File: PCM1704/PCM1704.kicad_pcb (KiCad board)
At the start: 4 copper layers, 90 x 90 mm, 126 parts, among them IC1 LT3042, IC2 LT3042, J1 AUDIO OUT, J2 POWER, J3 PROG, J5 I2S IN, U1 PCM1704, U10 LM337, U12 LM317, U2 PCM1704, U3 DF1704, U4 OPA1611, U5 OPA1611, U6 LT3094, U7 ATtiny1614, U8 OPA1612, U9 OPA1612

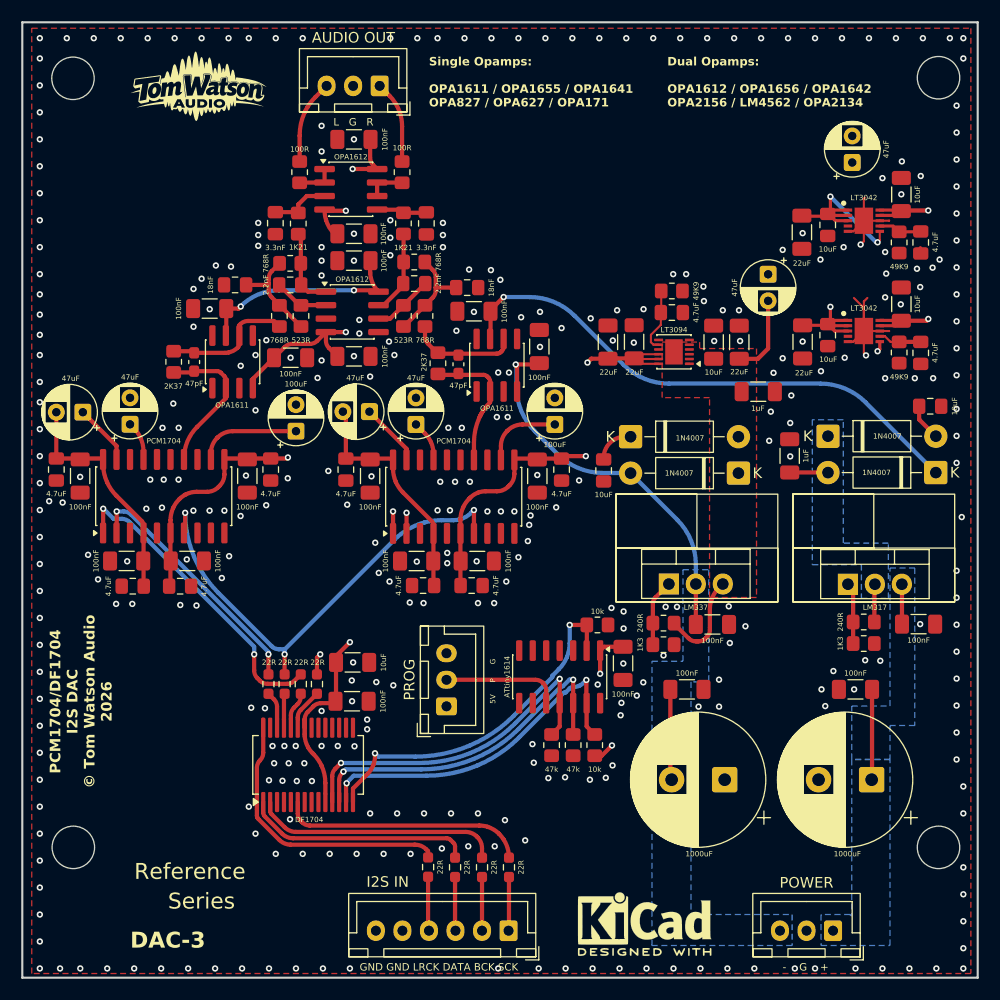
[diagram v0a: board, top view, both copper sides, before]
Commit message: PCM1704: snapshot before XMOS receive-buffer schematic changes
Adds DESIGN_REVIEW.md (performance review) and a manual zip backup.

Co-Authored-By: Claude Opus 5.5 <noreply@anthropic.com>
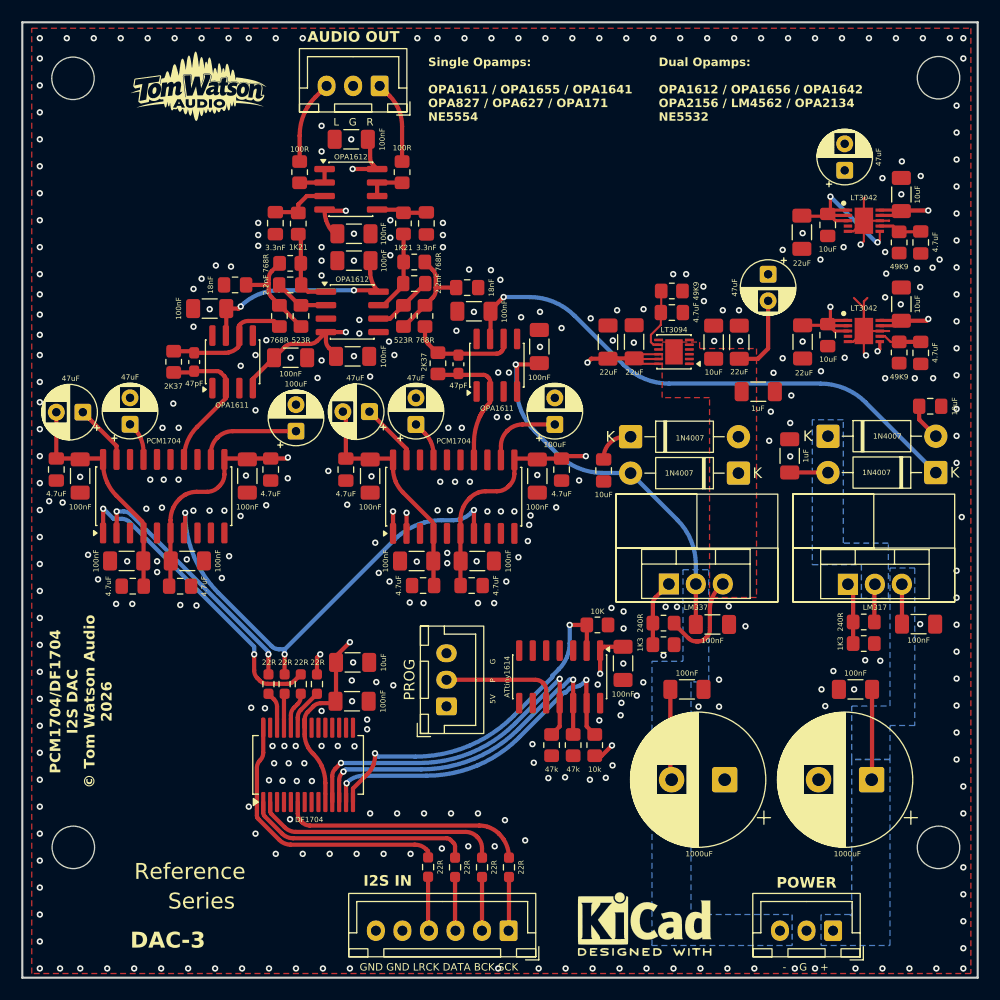
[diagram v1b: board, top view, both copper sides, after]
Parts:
- R75: value 10k -> 10K
- moved C22 1.02 mm to (188.2, 67.7)
- moved C86 0.25 mm to (141.7, 64.8)
- moved C85 0.13 mm to (141.9, 85.2)
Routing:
- net /+5VDF: track 165.0 -> 143.5 mm
- net /+8V: track 65.7 -> 64.2 mm
- net GND: track 22.4 -> 22.3 mm, vias 357 -> 358
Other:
- board text added: "Dual Opamps: OPA1612 / OPA1656 / OPA1642 OPA2156 / LM4562 / OPA2134 NE5532"
- board text added: "Single Opamps: OPA1611 / OPA1655 / OPA1641 OPA827 / OPA627 / OPA171 NE5554"
- board text removed: "Dual Opamps: OPA1612 / OPA1656 / OPA1642 OPA2156 / LM4562 / OPA2134"
- board text removed: "Single Opamps: OPA1611 / OPA1655 / OPA1641 OPA827 / OPA627 / OPA171"

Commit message: PCM1704: XMOS receive buffer, GND vias, WCLK re-route, 68R DF1704 series resistors
- Add U11 (74LVC1G17) MCLK Schmitt buffer, U13 (74LVC125APW) for BCK/DATA/LRCK,
  U14 (TPS7A2033) 3V3 rail; DF1704 inputs renamed DF_*
- GND vias at new ICs and decoupling caps; fix U13 pad 10 clearance
- Re-route WCLK on B.Cu so it no longer runs under BCLK on In2
- R79-R82 22R -> 68R (DF1704 SBAS099A 50-100R guidance), note updated
- DESIGN_REVIEW.md: H3 decision, LT3094 verification, change log

Co-Authored-By: Claude Opus 5.5 <noreply@anthropic.com>
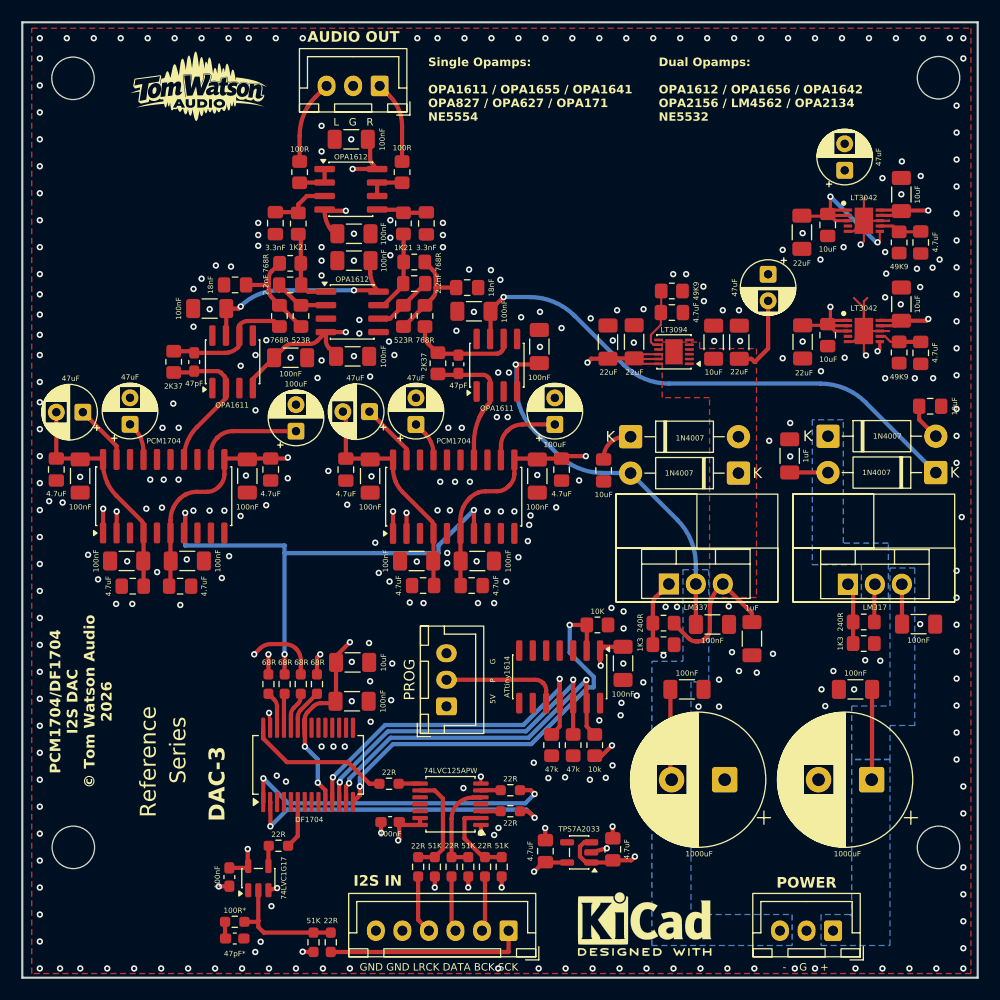
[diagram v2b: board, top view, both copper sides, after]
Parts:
- added C108: 100nF, Capacitor_SMD:C_0603_1608Metric_Pad1.08x0.95mm_HandSolder, F.Cu at (130.3, 134.3)
- added C109: 100nF, Capacitor_SMD:C_0603_1608Metric_Pad1.08x0.95mm_HandSolder, F.Cu at (145.4, 129.1)
- added C110: 4.7uF, Capacitor_SMD:C_0805_2012Metric_Pad1.18x1.45mm_HandSolder, F.Cu at (166.4, 131.7)
- added C111: 4.7uF, Capacitor_SMD:C_0805_2012Metric_Pad1.18x1.45mm_HandSolder, F.Cu at (160.0, 131.8)
- added C112: 47pF*, Capacitor_SMD:C_0603_1608Metric_Pad1.08x0.95mm_HandSolder, F.Cu at (130.8, 140.1)
- added R83: 51K, Resistor_SMD:R_0603_1608Metric_Pad0.98x0.95mm_HandSolder, F.Cu at (138.2, 140.4)
- added R84: 51K, Resistor_SMD:R_0603_1608Metric_Pad0.98x0.95mm_HandSolder, F.Cu at (155.9, 133.3)
- added R85: 51K, Resistor_SMD:R_0603_1608Metric_Pad0.98x0.95mm_HandSolder, F.Cu at (152.8, 133.3)
- added R86: 51K, Resistor_SMD:R_0603_1608Metric_Pad0.98x0.95mm_HandSolder, F.Cu at (149.6, 133.3)
- added R87: 22R, Resistor_SMD:R_0603_1608Metric_Pad0.98x0.95mm_HandSolder, F.Cu at (134.9, 131.3)
- added R88: 22R, Resistor_SMD:R_0603_1608Metric_Pad0.98x0.95mm_HandSolder, F.Cu at (156.7, 128.1)
- added R89: 22R, Resistor_SMD:R_0603_1608Metric_Pad0.98x0.95mm_HandSolder, F.Cu at (156.7, 126.1)
- added R90: 22R, Resistor_SMD:R_0603_1608Metric_Pad0.98x0.95mm_HandSolder, F.Cu at (145.3, 125.5)
- added R91: 100R*, Resistor_SMD:R_0603_1608Metric_Pad0.98x0.95mm_HandSolder, F.Cu at (130.8, 138.5)
- added U11: 74LVC1G17, Package_TO_SOT_SMD:SOT-23-5, F.Cu at (133.0, 134.4)
- added U13: 74LVC125APW, Package_SO:TSSOP-14_4.4x5mm_P0.65mm, F.Cu at (151.1, 127.4)
- added U14: TPS7A2033, Package_TO_SOT_SMD:SOT-23-5, F.Cu at (163.2, 131.9)
- R79, R80, R81, R82: value 22R -> 68R
- moved C90 23.3 mm to (179.5, 111.8), turned to -90 degrees
- moved R31 18.2 mm to (139.8, 140.4)
- moved R28 0.94 mm to (148.0, 133.3)
- moved R29 0.33 mm to (151.2, 133.3)
- moved R30 0.28 mm to (154.3, 133.3)
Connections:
- U3 pad 1: /DATAIN -> /DF_DIN
- U3 pad 2: /BCKIN -> /DF_BCK
- U3 pad 28: /LRCKIN -> /DF_LRCK
- U3 pad 6: /SCKIN -> /DF_SCK
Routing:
- net /+3V3: track 0.00 -> 42.0 mm, vias 0 -> 3
- net /DF_DIN: track 0.00 -> 30.6 mm, vias 0 -> 2
- net /DF_BCK: track 0.00 -> 29.8 mm, vias 0 -> 2
- net /+5VDF: track 143.5 -> 162.6 mm, vias 4 -> 7
- net /LRCKIN: track 27.2 -> 9.88 mm
- net /BCKIN: track 23.4 -> 7.69 mm
- net /DF_LRCK: track 0.00 -> 13.7 mm
- net Net-(J5-Pin_1): track 5.07 -> 18.8 mm
- net GND: track 22.3 -> 35.9 mm, vias 358 -> 343
- net /DATAIN: track 21.5 -> 9.02 mm
- net /SCKIN: track 23.4 -> 11.9 mm
- net /-8V: track 18.3 -> 23.3 mm
- net /DF_RST: track 34.2 -> 39.0 mm
- net /DF_SCK: track 0.00 -> 4.50 mm
- net Net-(U1-WCLK): track 46.1 -> 48.7 mm
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
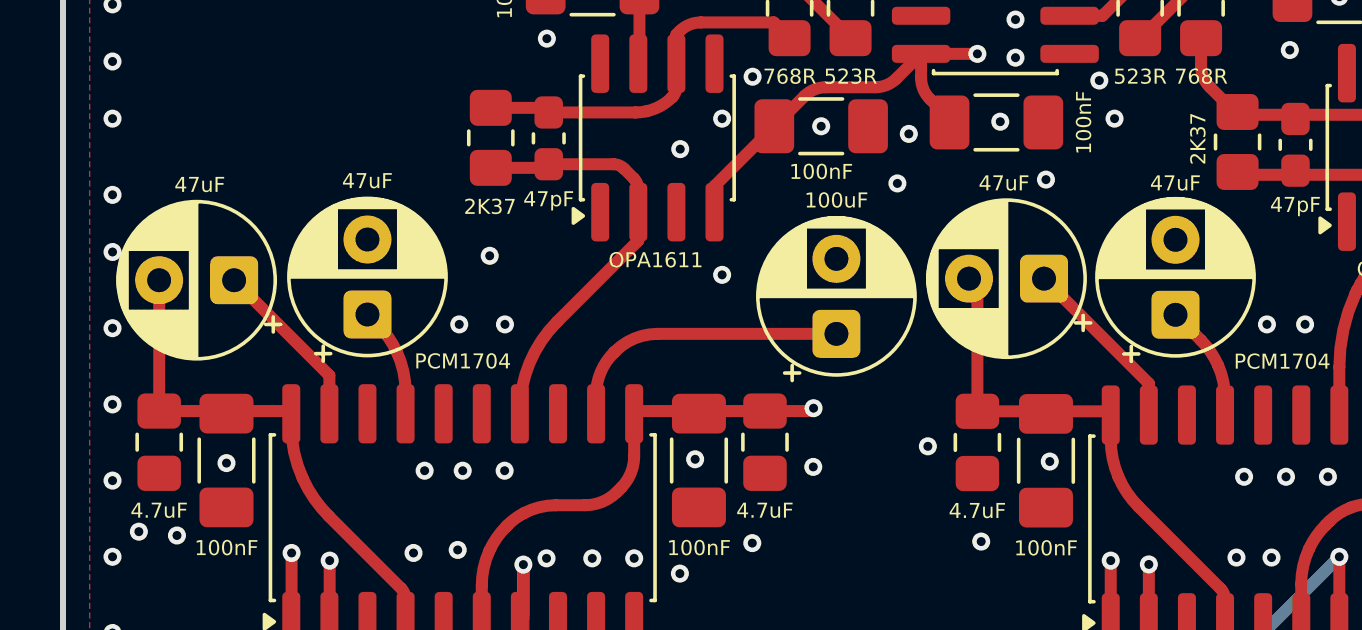
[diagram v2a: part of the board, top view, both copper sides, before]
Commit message: PCM1704: H2 - REF/SERVO caps no longer on the -5V supply trunk
-5V In2 trunk now feeds each PCM1704 via a dedicated via beside pin 20;
C16->C15 and C14->C13 negative returns linked on F.Cu to pin 20 node.
DRC (zones refilled) shows only pre-existing items.

Co-Authored-By: Claude Opus 5.5 <noreply@anthropic.com>
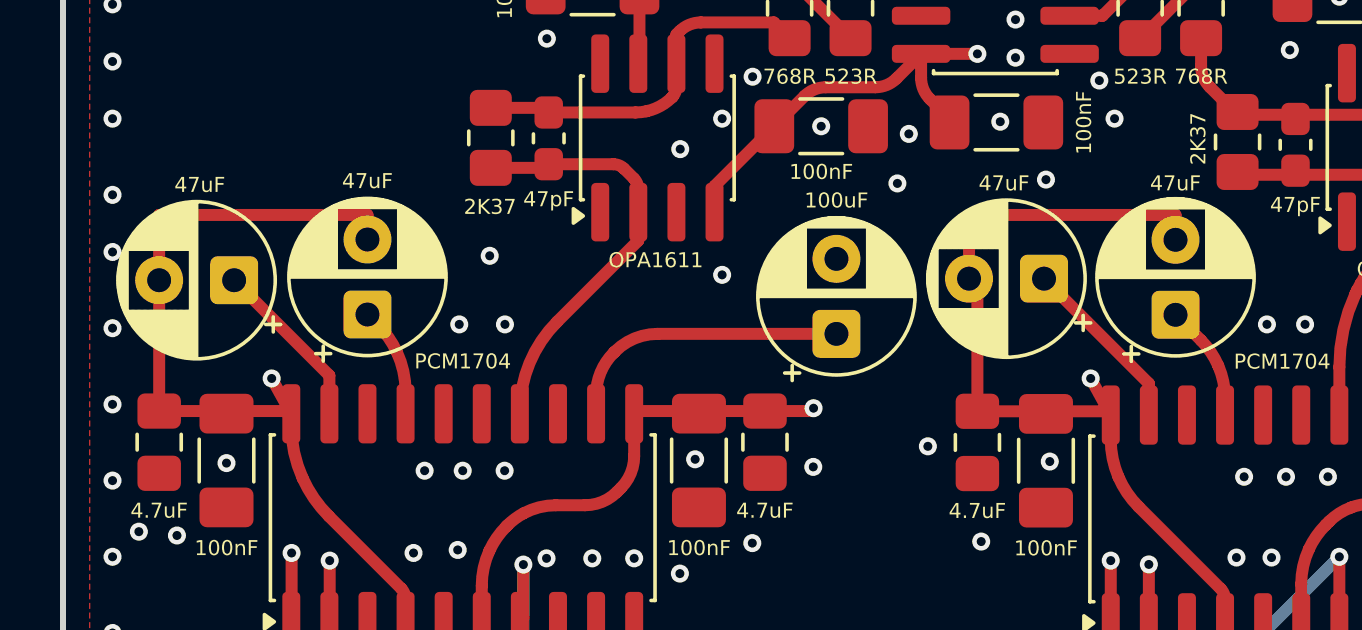
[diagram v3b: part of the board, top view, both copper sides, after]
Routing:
- net /-5V: track 111.5 -> 132.1 mm, vias 1 -> 3
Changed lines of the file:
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@@
+	)
+	(segment
+		(start 113.9483 88.3)
+		(end 113.9483 90.4756)
+		(width 0.4)
+		(layer "F.Cu")
+		(net "/-5V")
 	)
 	(segment
@@
 	)
 	(segment
+		(start 147.828 89.1291)
+		(end 147.828 88.3)
+		(width 0.4)
+		(layer "F.Cu")
+		(net "/-5V")
+	)
+	(segment
 		(start 145.669 94.9701)
 		(end 145.669 95.784809)
@@
 	)
 	(segment
+		(start 140.9451 88.3)
+		(end 140.9451 90.424)
+		(width 0.4)
+		(layer "F.Cu")
+		(net "/-5V")
+	)
+	(segment
 		(start 113.95026 94.8368)
 		(end 118.26186 94.8368)
@@
 	)
 	(segment
+		(start 120.8933 88.3)
+		(end 113.9483 88.3)
+		(width 0.4)
+		(layer "F.Cu")
+		(net "/-5V")
+	)
+	(segment
 		(start 122.16326 106.8447)
 		(end 122.18476 106.8662)
@@
 	)
 	(segment
+		(start 145 93.75)
+		(end 145.669 94.9701)
+		(width 0.4)
+		(layer "F.Cu")
+		(net "/-5V")
+	)
+	(segment
 		(start 122.16326 101.104307)
 		(end 122.16326 101.8532)
@@
 	)
 	(segment
+		(start 120.8933 89.1186)
+		(end 120.8933 88.3)
+		(width 0.4)
+		(layer "F.Cu")
+		(net "/-5V")
+	)
+	(segment
 		(start 122.16326 101.8532)
 		(end 122.16326 106.8447)
@@
 	)
 	(segment
+		(start 117.7 93.75)
+		(end 118.3533 94.9282)
+		(width 0.4)
+		(layer "F.Cu")
+		(net "/-5V")
+	)
+	(segment
 		(start 170.6836 85.9151)
 		(end 168.8846 85.9151)
@@
 		(width 0.4)
 		(layer "F.Cu")
+		(net "/-5V")
+	)
+	(segment
+		(start 147.828 88.3)
+		(end 140.9451 88.3)
+		(width 0.4)
+		(layer "F.Cu")
+		(net "/-5V")
+	)
+	(via
+		(at 145 93.75)
+		(size 0.6)
+		(drill 0.3)
+		(layers "F.Cu" "B.Cu")
 		(net "/-5V")
 	)
@@
 		(net "/-5V")
 	)
+	(via
+		(at 117.7 93.75)
+		(size 0.6)
+		(drill 0.3)
+		(layers "F.Cu" "B.Cu")
+		(net "/-5V")
+	)
 	(arc
 		(start 145.669 95.784809)
@@
 	)
 	(segment
-		(start 120.89326 89.1186)
-		(end 120.77626 89.0016)
-		(width 0.4)
-		(layer "In2.Cu")
-		(net "/-5V")
-	)
-	(segment
-		(start 147.828 89.129113)
-		(end 147.268687 88.5698)
-		(width 0.4)
-		(layer "In2.Cu")
-		(net "/-5V")
-	)
-	(segment
-		(start 120.77626 89.0016)
-		(end 113.94826 89.0016)
-		(width 0.4)
-		(layer "In2.Cu")
-		(net "/-5V")
-	)
-	(segment
-		(start 120.89326 89.1186)
-		(end 121.447747 88.564113)
-		(width 0.4)
-		(layer "In2.Cu")
-		(net "/-5V")
-	)
-	(segment
-		(start 137.027744 88.5698)
-		(end 140.945113 88.5698)
+		(start 145 93.75)
+		(end 117.7 93.75)
+		(width 0.4)
+		(layer "In2.Cu")
+		(net "/-5V")
+	)
+	(segment
+		(start 145 87.441)
+		(end 145 93.75)
 		(width 0.4)
 		(layer "In2.Cu")
@@
 	)
 	(segment
-		(start 140.945113 88.5698)
-		(end 140.945113 90.424)
-		(width 0.4)
-		(layer "In2.Cu")
-		(net "/-5V")
-	)
-	(segment
-		(start 137.022057 88.564113)
-		(end 137.027744 88.5698)
-		(width 0.4)
-		(layer "In2.Cu")
-		(net "/-5V")
-	)
-	(segment
-		(start 113.94826 89.0016)
-		(end 113.94826 90.4756)
-		(width 0.4)
-		(layer "In2.Cu")
-		(net "/-5V")
-	)
-	(segment
 		(start 163.9824 85.8012)
 		(end 162.3426 87.441)
@@
 	)
 	(segment
-		(start 121.447747 88.564113)
-		(end 137.022057 88.564113)
-		(width 0.4)
-		(layer "In2.Cu")
-		(net "/-5V")
-	)
-	(segment
-		(start 149.516113 87.441)
-		(end 147.828 89.129113)
-		(width 0.4)
-		(layer "In2.Cu")
-		(net "/-5V")
-	)
-	(segment
-		(start 147.268687 88.5698)
-		(end 140.945113 88.5698)
-		(width 0.4)
-		(layer "In2.Cu")
+		(start 149.5161 87.441)
+		(end 145 87.441)
+		(width 0.4)
+		(layer "In2.Cu")
